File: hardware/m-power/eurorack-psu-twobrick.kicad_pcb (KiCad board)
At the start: 2 copper layers, 29.8 x 108.7 mm, 24 parts, among them J1 12V wart A, J2 12V wart B, J3 USB-A 5V out, J5 Mini-Fit out, J6 Mini-Fit out, SW1 DPDT toggle (wired DPST)

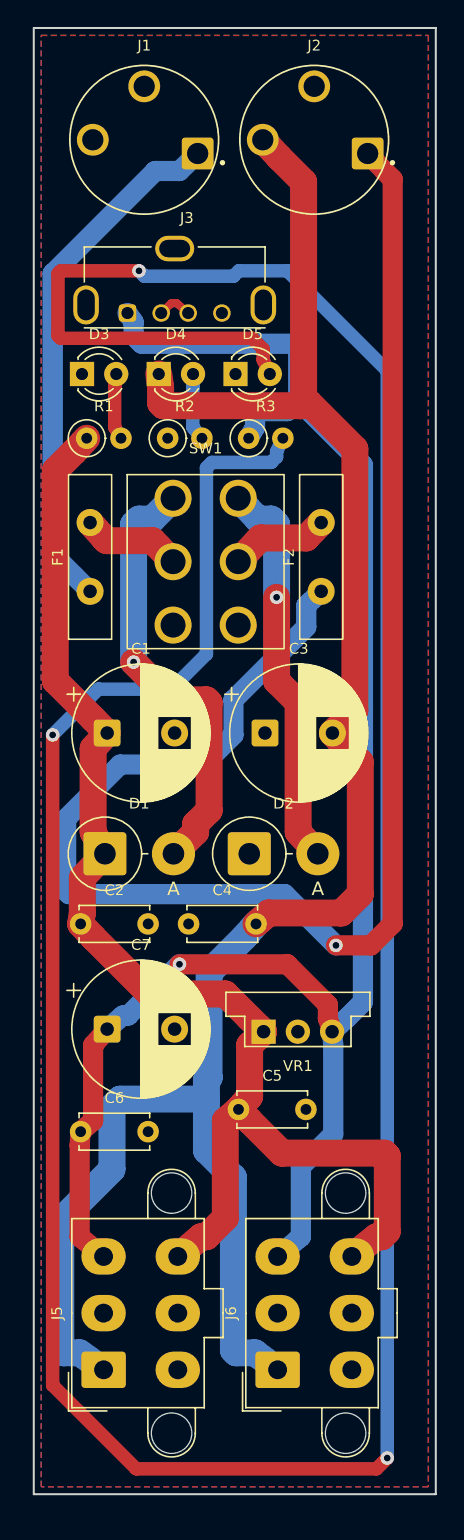
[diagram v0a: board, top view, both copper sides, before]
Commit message: Port Grains firmwares, experimental hardware
* fixing font width
* Fixing bugs in tides, slightly changing modes
* port 13 grains firmwares (Sean Luke, Apache 2.0) to mod1/mod2, learn from grains bit/fold/pluck in bitcrusher/wavefolder/karplus
* Merge branch 'tides-rework' into grains-ports
* real mod1/mod2 faceplates for the 13 grains ports; fit Rack widgets to the hole grid
* define braids Settings::CheckPaques stub so the plugin dylib actually dlopens
* braids: persist engine selection to flash, 10s hold resets to first engine with 5 LED flashes
* hardware experiments
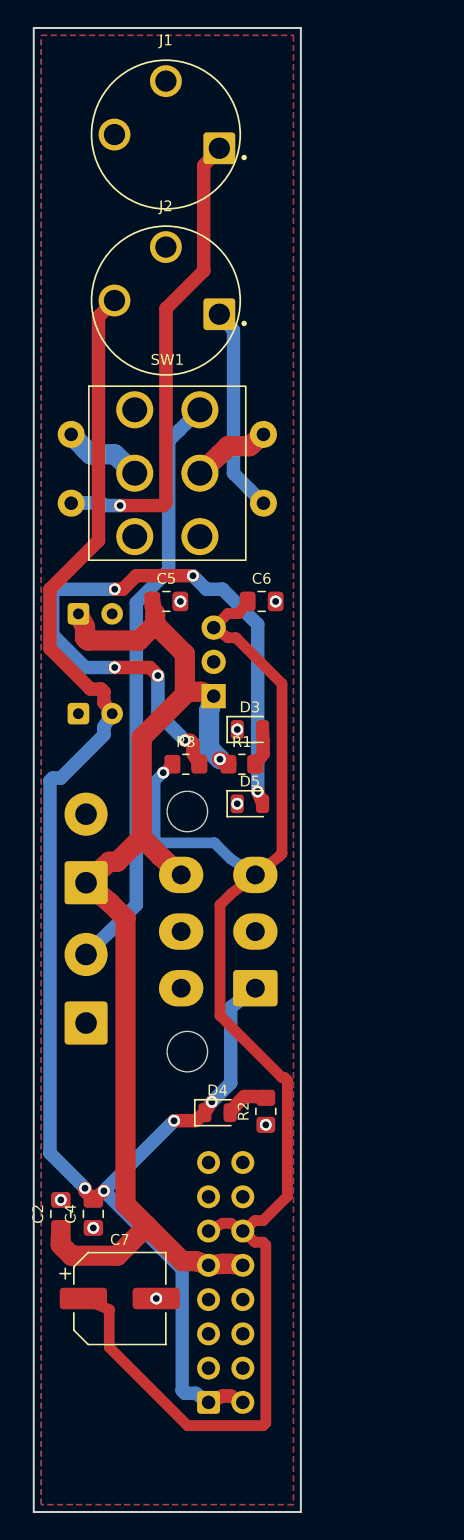
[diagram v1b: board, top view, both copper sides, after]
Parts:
- removed J3: USB-A 5V out, USB_A_Molex_105057_Vertical
- C1, C3: footprint CP_Radial_D10.0mm_P5.00mm -> CP_Radial_D6.3mm_P2.50mm; moved to B.Cu
- C2, C4, C5, C6: footprint C_Disc_D5.0mm_W2.5mm_P5.00mm -> C_0805_2012Metric_Pad1.18x1.45mm_HandSolder
- C7: value 47uF 100V -> 47uF 63V; footprint CP_Radial_D10.0mm_P5.00mm -> CP_Elec_6.3x7.7
- D1, D2, F1, F2, J5, VR1: moved to B.Cu
- D3: value LED white +12V -> LED white 0805 +12V; footprint LED_D3.0mm -> LED_0805_2012Metric
- D4: value LED pink -12V -> LED pink 0805 -12V; footprint LED_D3.0mm -> LED_0805_2012Metric
- D5: value LED blue +5V -> LED blue 0805 +5V; footprint LED_D3.0mm -> LED_0805_2012Metric
- J6: value Mini-Fit out -> Eurorack 16-pin out; footprint Molex_Mini-Fit_Jr_5566-06A2_2x03_P4.20mm_Vertical -> IDC-Header_2x08_P2.54mm_Vertical; moved to B.Cu
- R1, R2, R3: footprint R_Axial_DIN0207_L6.3mm_D2.5mm_P2.54mm_Vertical -> R_0805_2012Metric_Pad1.20x1.40mm_HandSolder
- moved D4 54.9 mm to (13.6, 80.4)
- moved R2 50.4 mm to (17.2, 80.3), turned to 90 degrees
- moved C6 41.5 mm to (16.9, 42.5)
- moved C5 38.0 mm to (9.83, 42.5)
- moved D5 31.9 mm to (16.0, 57.5)
- moved J5 30.4 mm to (16.4, 71.2)
- moved D3 29.1 mm to (16.0, 52.0)
- moved R1 26.8 mm to (15.4, 54.6)
- moved VR1 25.1 mm to (13.3, 49.5), turned to 90 degrees
- moved R3 24.6 mm to (11.3, 54.6)
- moved C4 22.6 mm to (4.41, 87.9), turned to 90 degrees
- moved C2 21.5 mm to (2.00, 87.9), turned to 90 degrees
- moved C7 20.0 mm to (6.38, 94.2)
- moved D2 17.4 mm to (3.88, 73.8), turned to 90 degrees
- moved J2 16.2 mm to (9.79, 20.2)
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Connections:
- J6 pad 2: GND -> -12V
- J6 pad 3: +5V -> GND
- J6 pad 6: +12V -> GND
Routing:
- net N_L3: track 241.3 -> 50.8 mm, vias 3 -> 6
- net VIN_B: track 118.1 -> 15.3 mm, vias 1 -> 0
- net N_SA: track 33.1 -> 0.00 mm, vias 1 -> 0
- net -12V: track 150.2 -> 118.4 mm, vias 0 -> 4
- net +5V: track 132.2 -> 108.5 mm
- net N_SB: track 29.3 -> 43.9 mm, vias 1 -> 0
- net +12V: track 97.7 -> 89.4 mm, vias 0 -> 1
- net VIN_A: track 39.1 -> 35.1 mm, vias 0 -> 1
- net USB_DP: track 2.56 -> 0.00 mm
- net N_L1: track 4.89 -> 2.77 mm
- net N_L2: track 5.00 -> 3.20 mm
- net N_FB: track 7.40 -> 5.84 mm
- net N_FA: track 7.40 -> 5.89 mm
- net GND: vias 0 -> 8
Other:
- board size 29.8 x 108.7 mm -> 19.8 x 110 mm
